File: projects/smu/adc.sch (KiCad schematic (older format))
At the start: 30 parts, among them U301 LM741, U304 LM741, U305 LM311N, U8 DG444, U9 LM741

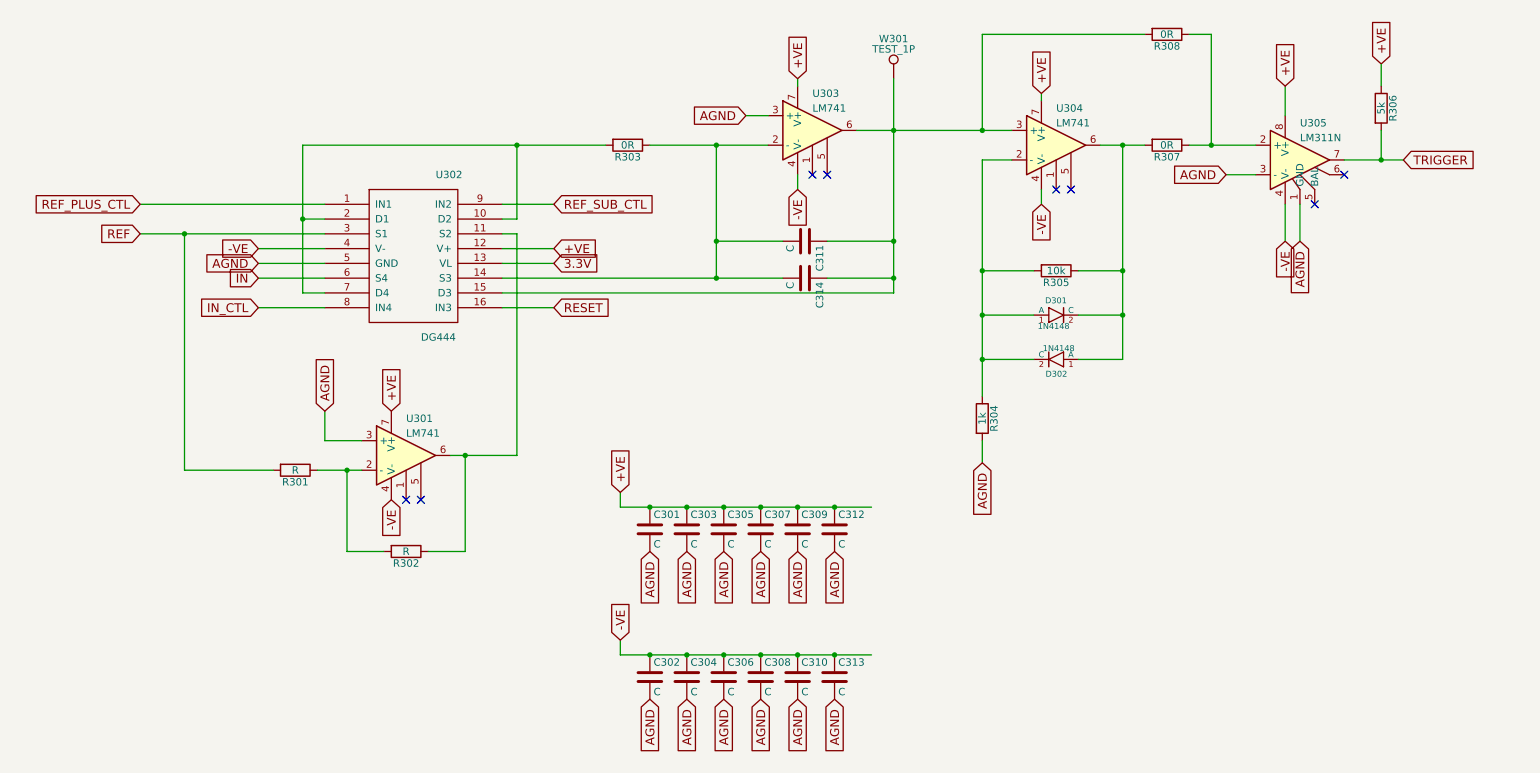
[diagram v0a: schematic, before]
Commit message: renaming pins
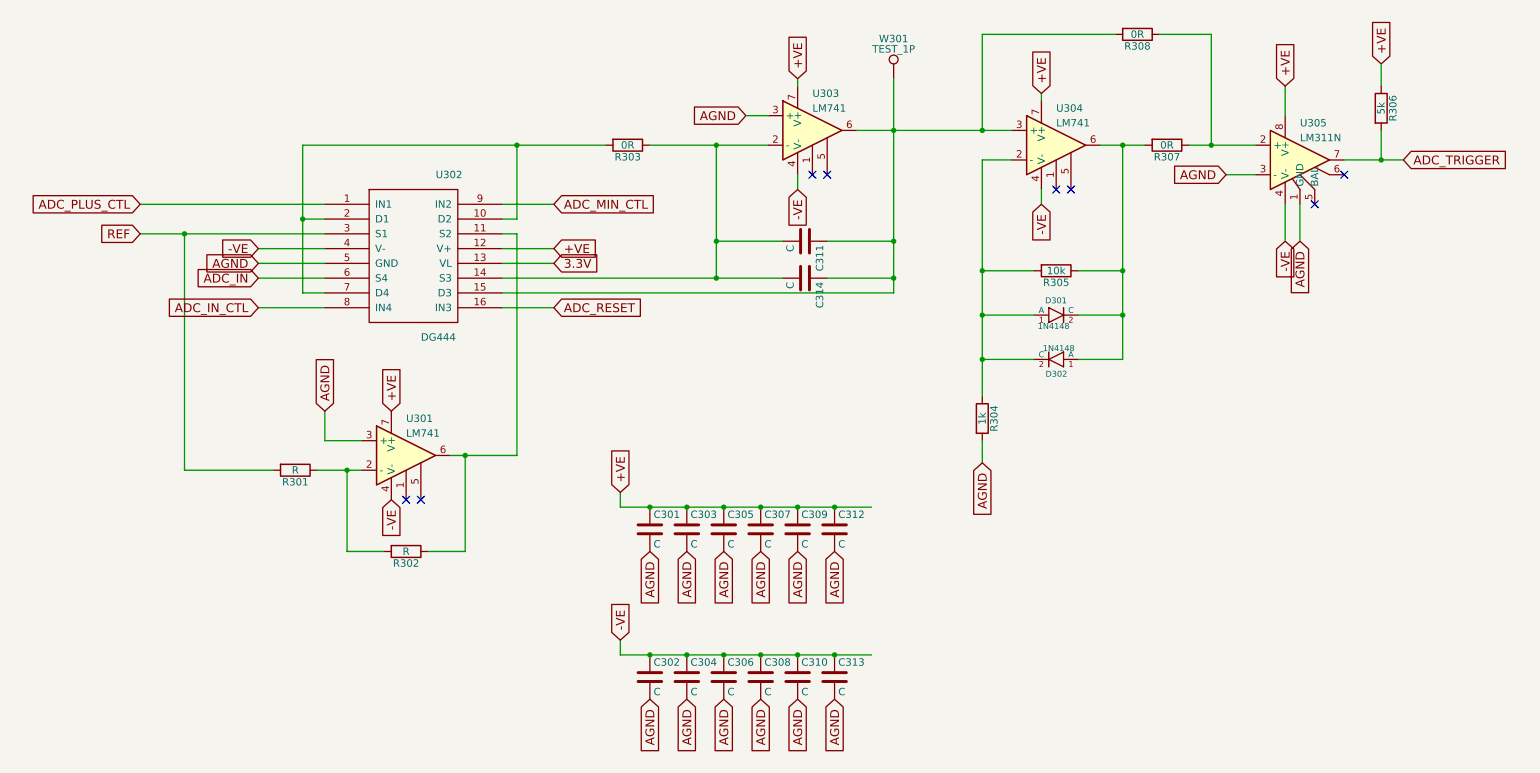
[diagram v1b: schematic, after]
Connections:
- net IN renamed ADC_IN
- net IN_CTL renamed ADC_IN_CTL
- net REF_PLUS_CTL renamed ADC_PLUS_CTL
- net REF_SUB_CTL renamed ADC_MIN_CTL
- net RESET renamed ADC_RESET
- net TRIGGER renamed ADC_TRIGGER
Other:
- moved on the sheet: R308
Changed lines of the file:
@@
 REF
 Text GLabel 4450 3200 2    60   Input ~ 0
-RESET
+ADC_RESET
 Text GLabel 4450 2900 2    60   Input ~ 0
 3.3V
@@
 AGND
 Text GLabel 2450 3200 0    60   Input ~ 0
-IN_CTL
+ADC_IN_CTL
 Text GLabel 6100 1650 1    60   Input ~ 0
 +VE
@@
 AGND
 Text GLabel 1650 2500 0    60   Input ~ 0
-REF_PLUS_CTL
+ADC_PLUS_CTL
 Text GLabel 4450 2500 2    60   Input ~ 0
-REF_SUB_CTL
+ADC_MIN_CTL
 Text GLabel 2450 3000 0    60   Input ~ 0
-IN
+ADC_IN
 $Comp
 L C C311
@@
 AGND
 Text GLabel 10200 2200 2    60   Input ~ 0
-TRIGGER
+ADC_TRIGGER
 Wire Wire Line
 	4100 2800 4450 2800
@@
 L R R308
 U 1 1 58A97AC8
-P 8600 1350
-F 0 "R308" V 8680 1350 50  0000 C CNN
-F 1 "0R" V 8600 1350 50  0000 C CNN
-F 2 "Resistors_SMD:R_1206" V 8530 1350 50  0001 C CNN
-F 3 "" H 8600 1350 50  0000 C CNN
-	1    8600 1350
-	0    1    1    0
-$EndComp
-Wire Wire Line
-	8450 1350 7350 1350
-Wire Wire Line
-	8750 1350 8900 1350
+P 8400 1350
+F 0 "R308" V 8480 1350 50  0000 C CNN
+F 1 "0R" V 8400 1350 50  0000 C CNN
+F 2 "Resistors_SMD:R_1206" V 8330 1350 50  0001 C CNN
+F 3 "" H 8400 1350 50  0000 C CNN
+	1    8400 1350
+	0    1    1    0
+$EndComp
+Wire Wire Line
+	8250 1350 7350 1350
+Wire Wire Line
+	8550 1350 8900 1350
 Wire Wire Line
 	8900 1350 8900 2100
